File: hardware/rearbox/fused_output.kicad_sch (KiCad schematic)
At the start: 15 parts, among them U7 VND7020AJTR

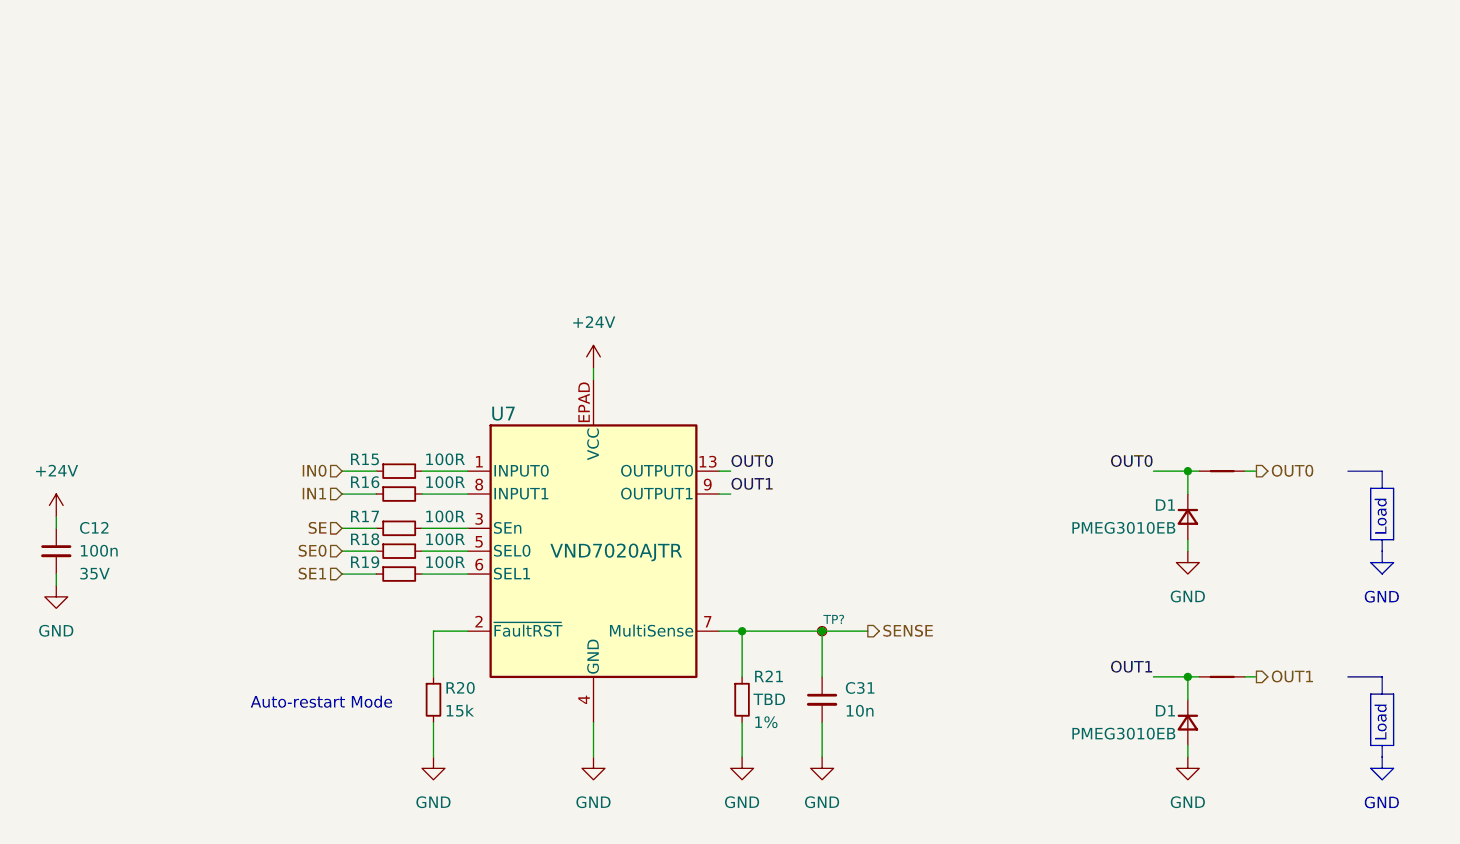
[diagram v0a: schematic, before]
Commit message: Place components on the PCB
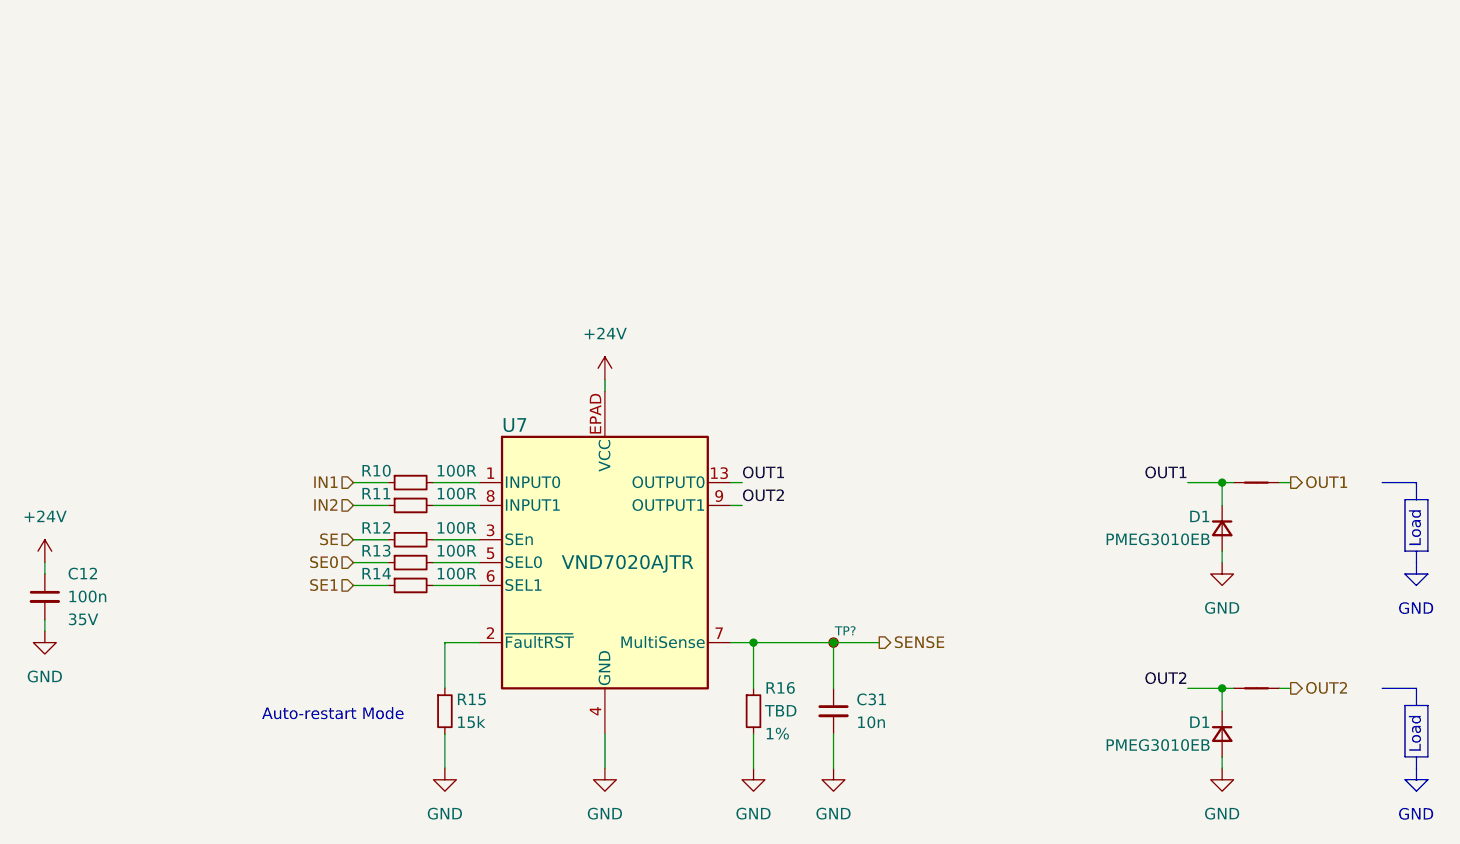
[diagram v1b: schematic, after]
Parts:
- renumbered R15 to R10, R16 to R11, R17 to R12, R18 to R13, R19 to R14, R20 to R15, R21 to R16
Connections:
- net IN0 is gone; now on net IN1: R10.1
- net OUT0 is gone; now on net OUT1: D1.1 (K), NT5.1, NT5.2, U7.13 (OUTPUT0), U7.14 (OUTPUT0), U7.15 (OUTPUT0), U7.16 (OUTPUT0)
- net IN1: no longer R11.1
- net OUT1: no longer D1.1 (K), NT5.1, NT5.2, U7.10 (OUTPUT1), U7.11 (OUTPUT1), U7.12 (OUTPUT1), U7.9 (OUTPUT1)
- new net IN2: R11.1
- new net OUT2: D1.1 (K), NT5.1, NT5.2, U7.10 (OUTPUT1), U7.11 (OUTPUT1), U7.12 (OUTPUT1), U7.9 (OUTPUT1)
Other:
- moved on the sheet: C12, C31, D1, R10, R11, R12, R13, R14, R15, R16, TP?, U7

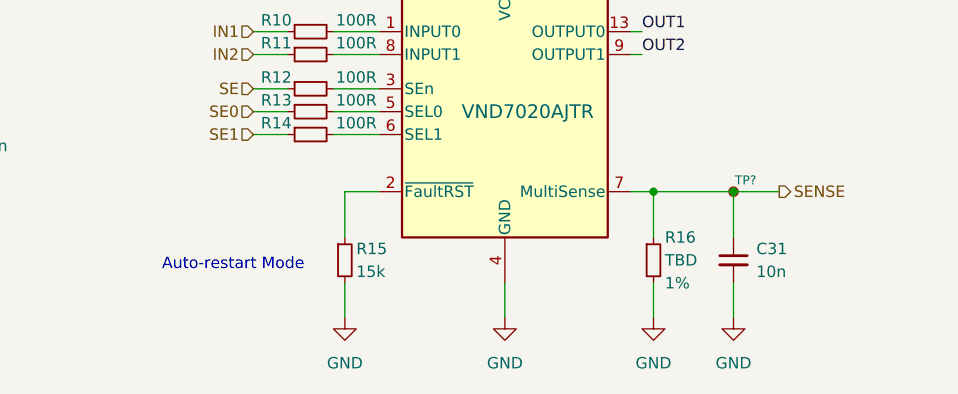
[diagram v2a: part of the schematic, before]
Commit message: Route PCB tracks
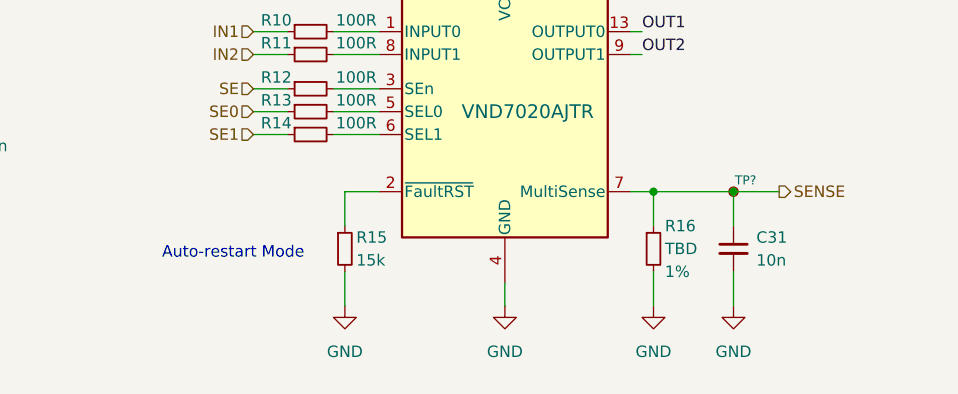
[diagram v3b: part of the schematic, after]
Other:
- moved on the sheet: C31, R15, R16
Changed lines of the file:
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@@
     (stroke (width 0) (type default))
   )
-  (wire (pts (xy 119.38 113.03) (xy 119.38 116.84))
+  (wire (pts (xy 119.38 111.76) (xy 119.38 115.57))
     (stroke (width 0) (type default))
   )
@@
     (stroke (width 0) (type default))
   )
-  (wire (pts (xy 162.56 102.87) (xy 162.56 107.95))
+  (wire (pts (xy 162.56 102.87) (xy 162.56 106.68))
     (stroke (width 0) (type default))
   )
@@
     (stroke (width 0) (type default))
   )
-  (wire (pts (xy 162.56 113.03) (xy 162.56 116.84))
-    (stroke (width 0) (type default))
-  )
-  (wire (pts (xy 153.67 102.87) (xy 153.67 107.95))
+  (wire (pts (xy 162.56 111.76) (xy 162.56 115.57))
+    (stroke (width 0) (type default))
+  )
+  (wire (pts (xy 153.67 102.87) (xy 153.67 106.68))
     (stroke (width 0) (type default))
   )
@@
     (stroke (width 0) (type default))
   )
-  (wire (pts (xy 137.16 113.03) (xy 137.16 116.84))
+  (wire (pts (xy 137.16 113.03) (xy 137.16 115.57))
     (stroke (width 0) (type default))
   )
@@
     (stroke (width 0) (type default))
   )
+  (wire (pts (xy 153.67 111.76) (xy 153.67 115.57))
+    (stroke (width 0) (type default))
+  )
   (polyline (pts (xy 223.52 85.09) (xy 227.33 85.09))
     (stroke (width 0) (type default))
@@
     (stroke (width 0) (type default))
   )
-  (wire (pts (xy 119.38 102.87) (xy 119.38 107.95))
+  (wire (pts (xy 119.38 102.87) (xy 119.38 106.68))
     (stroke (width 0) (type default))
   )
@@
   )
   (wire (pts (xy 153.67 102.87) (xy 162.56 102.87))
-    (stroke (width 0) (type default))
-  )
-  (wire (pts (xy 153.67 113.03) (xy 153.67 116.84))
     (stroke (width 0) (type default))
   )
@@
     (effects (font (size 1.27 1.27)) (justify left bottom))
   )
-  (text "Auto-restart Mode" (at 99.06 111.76 0)
+  (text "Auto-restart Mode" (at 99.06 110.49 0)
     (effects (font (size 1.27 1.27)) (justify left bottom))
   )
@@
     )
   )
-  (symbol (lib_id "power:GND") (at 162.56 116.84 0) (unit 1)
-    (in_bom yes) (on_board yes) (dnp no)
-    (property "Reference" "#PWR?" (at 162.56 123.19 0)
-      (effects (font (size 1.27 1.27)) hide)
-    )
-    (property "Value" "GND" (at 162.56 121.92 0)
-      (effects (font (size 1.27 1.27)))
-    )
-    (property "Footprint" "" (at 162.56 116.84 0)
-      (effects (font (size 1.27 1.27)) hide)
-    )
-    (property "Datasheet" "" (at 162.56 116.84 0)
+  (symbol (lib_id "power:GND") (at 162.56 115.57 0) (unit 1)
+    (in_bom yes) (on_board yes) (dnp no)
+    (property "Reference" "#PWR?" (at 162.56 121.92 0)
+      (effects (font (size 1.27 1.27)) hide)
+    )
+    (property "Value" "GND" (at 162.56 120.65 0)
+      (effects (font (size 1.27 1.27)))
+    )
+    (property "Footprint" "" (at 162.56 115.57 0)
+      (effects (font (size 1.27 1.27)) hide)
+    )
+    (property "Datasheet" "" (at 162.56 115.57 0)
       (effects (font (size 1.27 1.27)) hide)
     )
@@
     )
   )
-  (symbol (lib_id "Device:R_Small") (at 153.67 110.49 0) (unit 1)
-    (in_bom yes) (on_board yes) (dnp no)
-    (property "Reference" "R16" (at 154.94 107.95 0)
+  (symbol (lib_id "Device:R_Small") (at 153.67 109.22 0) (unit 1)
+    (in_bom yes) (on_board yes) (dnp no)
+    (property "Reference" "R16" (at 154.94 106.68 0)
       (effects (font (size 1.27 1.27)) (justify left))
     )
-    (property "Value" "TBD" (at 154.94 110.49 0)
+    (property "Value" "TBD" (at 154.94 109.22 0)
       (effects (font (size 1.27 1.27)) (justify left))
     )
-    (property "Footprint" "Resistor_SMD:R_0603_1608Metric" (at 153.67 110.49 0)
-      (effects (font (size 1.27 1.27)) hide)
-    )
-    (property "Datasheet" "~" (at 153.67 110.49 0)
-      (effects (font (size 1.27 1.27)) hide)
-    )
-    (property "Tolerance" "1%" (at 154.94 113.03 0)
+    (property "Footprint" "Resistor_SMD:R_0603_1608Metric" (at 153.67 109.22 0)
+      (effects (font (size 1.27 1.27)) hide)
+    )
+    (property "Datasheet" "~" (at 153.67 109.22 0)
+      (effects (font (size 1.27 1.27)) hide)
+    )
+    (property "Tolerance" "1%" (at 154.94 111.76 0)
       (effects (font (size 1.27 1.27)) (justify left))
     )
@@
     )
   )
-  (symbol (lib_id "power:GND") (at 153.67 116.84 0) (unit 1)
-    (in_bom yes) (on_board yes) (dnp no)
-    (property "Reference" "#PWR?" (at 153.67 123.19 0)
-      (effects (font (size 1.27 1.27)) hide)
-    )
-    (property "Value" "GND" (at 153.67 121.92 0)
-      (effects (font (size 1.27 1.27)))
-    )
-    (property "Footprint" "" (at 153.67 116.84 0)
-      (effects (font (size 1.27 1.27)) hide)
-    )
-    (property "Datasheet" "" (at 153.67 116.84 0)
+  (symbol (lib_id "power:GND") (at 153.67 115.57 0) (unit 1)
+    (in_bom yes) (on_board yes) (dnp no)
+    (property "Reference" "#PWR?" (at 153.67 121.92 0)
+      (effects (font (size 1.27 1.27)) hide)
+    )
+    (property "Value" "GND" (at 153.67 120.65 0)
+      (effects (font (size 1.27 1.27)))
+    )
+    (property "Footprint" "" (at 153.67 115.57 0)
+      (effects (font (size 1.27 1.27)) hide)
+    )
+    (property "Datasheet" "" (at 153.67 115.57 0)
       (effects (font (size 1.27 1.27)) hide)
     )
@@
     )
   )
-  (symbol (lib_id "Device:R_Small") (at 119.38 110.49 0) (unit 1)
-    (in_bom yes) (on_board yes) (dnp no)
-    (property "Reference" "R15" (at 120.65 109.22 0)
+  (symbol (lib_id "Device:R_Small") (at 119.38 109.22 0) (unit 1)
+    (in_bom yes) (on_board yes) (dnp no)
+    (property "Reference" "R15" (at 120.65 107.95 0)
       (effects (font (size 1.27 1.27)) (justify left))
     )
-    (property "Value" "15k" (at 120.65 111.76 0)
+    (property "Value" "15k" (at 120.65 110.49 0)
       (effects (font (size 1.27 1.27)) (justify left))
     )
-    (property "Footprint" "Resistor_SMD:R_0603_1608Metric" (at 119.38 110.49 0)
-      (effects (font (size 1.27 1.27)) hide)
-    )
-    (property "Datasheet" "~" (at 119.38 110.49 0)
+    (property "Footprint" "Resistor_SMD:R_0603_1608Metric" (at 119.38 109.22 0)
+      (effects (font (size 1.27 1.27)) hide)
+    )
+    (property "Datasheet" "~" (at 119.38 109.22 0)
       (effects (font (size 1.27 1.27)) hide)
     )
@@
     )
   )
-  (symbol (lib_id "power:GND") (at 137.16 116.84 0) (unit 1)
-    (in_bom yes) (on_board yes) (dnp no)
-    (property "Reference" "#PWR?" (at 137.16 123.19 0)
-      (effects (font (size 1.27 1.27)) hide)
-    )
-    (property "Value" "GND" (at 137.16 121.92 0)
-      (effects (font (size 1.27 1.27)))
-    )
-    (property "Footprint" "" (at 137.16 116.84 0)
-      (effects (font (size 1.27 1.27)) hide)
-    )
-    (property "Datasheet" "" (at 137.16 116.84 0)
+  (symbol (lib_id "power:GND") (at 137.16 115.57 0) (unit 1)
+    (in_bom yes) (on_board yes) (dnp no)
+    (property "Reference" "#PWR?" (at 137.16 121.92 0)
+      (effects (font (size 1.27 1.27)) hide)
+    )
+    (property "Value" "GND" (at 137.16 120.65 0)
+      (effects (font (size 1.27 1.27)))
+    )
+    (property "Footprint" "" (at 137.16 115.57 0)
+      (effects (font (size 1.27 1.27)) hide)
+    )
+    (property "Datasheet" "" (at 137.16 115.57 0)
       (effects (font (size 1.27 1.27)) hide)
     )
@@
     )
   )
-  (symbol (lib_id "power:GND") (at 119.38 116.84 0) (unit 1)
-    (in_bom yes) (on_board yes) (dnp no)
-    (property "Reference" "#PWR?" (at 119.38 123.19 0)
-      (effects (font (size 1.27 1.27)) hide)
-    )
-    (property "Value" "GND" (at 119.38 121.92 0)
-      (effects (font (size 1.27 1.27)))
-    )
-    (property "Footprint" "" (at 119.38 116.84 0)
-      (effects (font (size 1.27 1.27)) hide)
-    )
-    (property "Datasheet" "" (at 119.38 116.84 0)
+  (symbol (lib_id "power:GND") (at 119.38 115.57 0) (unit 1)
+    (in_bom yes) (on_board yes) (dnp no)
+    (property "Reference" "#PWR?" (at 119.38 121.92 0)
+      (effects (font (size 1.27 1.27)) hide)
+    )
+    (property "Value" "GND" (at 119.38 120.65 0)
+      (effects (font (size 1.27 1.27)))
+    )
+    (property "Footprint" "" (at 119.38 115.57 0)
+      (effects (font (size 1.27 1.27)) hide)
+    )
+    (property "Datasheet" "" (at 119.38 115.57 0)
       (effects (font (size 1.27 1.27)) hide)
     )
@@
     )
   )
-  (symbol (lib_id "Device:C_Small") (at 162.56 110.49 0) (unit 1)
+  (symbol (lib_id "Device:C_Small") (at 162.56 109.22 0) (unit 1)
     (in_bom yes) (on_board yes) (dnp no) (fields_autoplaced)
-    (property "Reference" "C31" (at 165.1 109.2263 0)
+    (property "Reference" "C31" (at 165.1 107.9563 0)
       (effects (font (size 1.27 1.27)) (justify left))
     )
-    (property "Value" "10n" (at 165.1 111.7663 0)
+    (property "Value" "10n" (at 165.1 110.4963 0)
       (effects (font (size 1.27 1.27)) (justify left))
     )
-    (property "Footprint" "Capacitor_SMD:C_0603_1608Metric" (at 162.56 110.49 0)
-      (effects (font (size 1.27 1.27)) hide)
-    )
-    (property "Datasheet" "~" (at 162.56 110.49 0)
-      (effects (font (size 1.27 1.27)) hide)
-    )
+    (property "Footprint" "Capacitor_SMD:C_0603_1608Metric" (at 162.56 109.22 0)
+      (effects (font (size 1.27 1.27)) hide)
+    )
+    (property "Datasheet" "~" (at 162.56 109.22 0)
+      (effects (font (size 1.27 1.27)) hide)
+    )

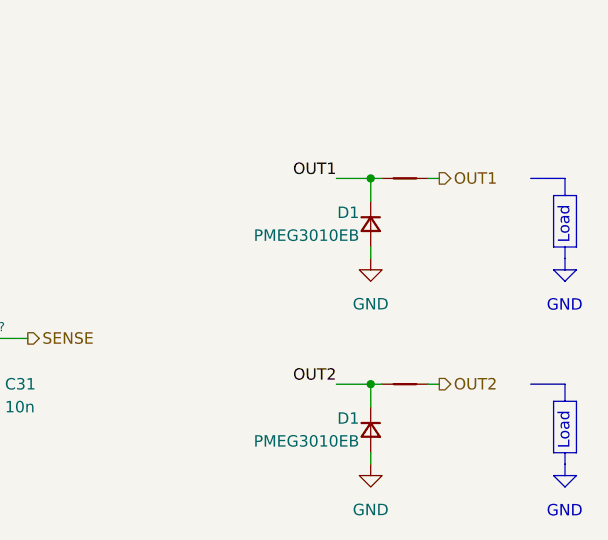
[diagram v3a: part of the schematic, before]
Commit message: Fix DRCs
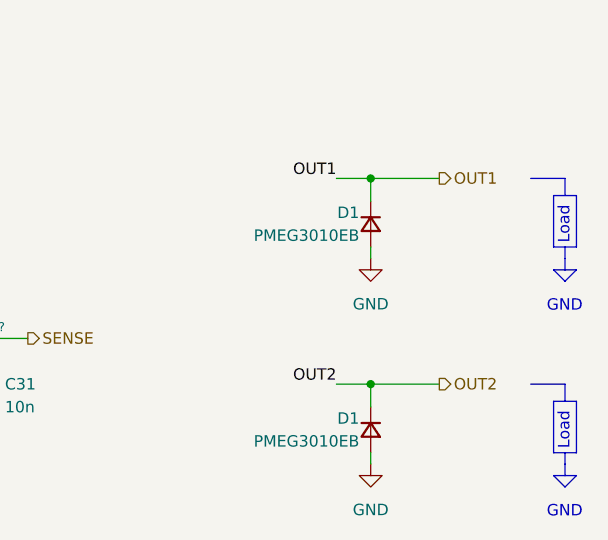
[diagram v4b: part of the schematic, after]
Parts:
- removed NT5 (x2): NetTie_2, NetTie:NetTie-2_SMD_Pad0.5mm, symbol Device:NetTie_2
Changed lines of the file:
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@@
   (title_block
     (title "Fans")
-    (date "2023-11-02")
+    (date "2023-11-17")
     (rev "${REVISION}")
     (company "Author: I. Kajdan")
@@
     (stroke (width 0) (type default))
   )
-  (wire (pts (xy 205.74 85.09) (xy 207.01 85.09))
-    (stroke (width 0) (type default))
-  )
   (polyline (pts (xy 226.06 95.25) (xy 227.33 95.25))
     (stroke (width 0) (type default))
@@
     (stroke (width 0) (type default))
   )
-  (wire (pts (xy 212.09 85.09) (xy 213.36 85.09))
+  (wire (pts (xy 205.74 85.09) (xy 213.36 85.09))
     (stroke (width 0) (type default))
   )
@@
     (stroke (width 0) (type default))
   )
-  (wire (pts (xy 212.09 107.95) (xy 213.36 107.95))
-    (stroke (width 0) (type default))
-  )
   (wire (pts (xy 205.74 85.09) (xy 205.74 87.63))
     (stroke (width 0) (type default))
@@
     (stroke (width 0) (type default))
   )
-  (wire (pts (xy 205.74 107.95) (xy 207.01 107.95))
+  (wire (pts (xy 205.74 107.95) (xy 213.36 107.95))
     (stroke (width 0) (type default))
   )
@@
     )
   )
-  (symbol (lib_id "Device:NetTie_2") (at 209.55 85.09 0) (unit 1)
-    (in_bom no) (on_board yes) (dnp no) (fields_autoplaced)
-    (property "Reference" "NT5" (at 209.55 80.01 0)
-      (effects (font (size 1.27 1.27)) hide)
-    )
-    (property "Value" "NetTie_2" (at 209.55 82.55 0)
-      (effects (font (size 1.27 1.27)) hide)
-    )
-    (property "Footprint" "NetTie:NetTie-2_SMD_Pad0.5mm" (at 209.55 85.09 0)
-      (effects (font (size 1.27 1.27)) hide)
-    )
-    (property "Datasheet" "~" (at 209.55 85.09 0)
-      (effects (font (size 1.27 1.27)) hide)
-    )
-    (pin "1")
-    (pin "2")
-    (instances
-      (project "rearbox"
-        (path "/b652b05a-4e3d-4ad1-b032-18886abe7d45/620acd23-76d3-49a1-9dab-637cd753e552"
-          (reference "NT5") (unit 1)
-        )
-        (path "/b652b05a-4e3d-4ad1-b032-18886abe7d45/12f12a63-cabc-40cf-a64b-d1bd8b3dd459"
-          (reference "NT1") (unit 1)
-        )
-        (path "/b652b05a-4e3d-4ad1-b032-18886abe7d45/2f82735d-d185-44cc-bb86-fc399780134d"
-          (reference "NT3") (unit 1)
-        )
-      )
-    )
-  )
   (symbol (lib_id "power:GND") (at 153.67 115.57 0) (unit 1)
     (in_bom yes) (on_board yes) (dnp no)
@@
         )
       )
-    )
-  )
-  (symbol (lib_id "Device:NetTie_2") (at 209.55 107.95 0) (unit 1)
-    (in_bom no) (on_board yes) (dnp no) (fields_autoplaced)
-    (property "Reference" "NT5" (at 209.55 102.87 0)
-      (effects (font (size 1.27 1.27)) hide)
-    )
-    (property "Value" "NetTie_2" (at 209.55 105.41 0)
-      (effects (font (size 1.27 1.27)) hide)
-    )
-    (property "Footprint" "NetTie:NetTie-2_SMD_Pad0.5mm" (at 209.55 107.95 0)
-      (effects (font (size 1.27 1.27)) hide)
-    )
-    (property "Datasheet" "~" (at 209.55 107.95 0)
-      (effects (font (size 1.27 1.27)) hide)
-    )
-    (pin "1")
-    (pin "2")
-    (instances
-      (project "rearbox"
-        (path "/b652b05a-4e3d-4ad1-b032-18886abe7d45/620acd23-76d3-49a1-9dab-637cd753e552"
-          (reference "NT5") (unit 1)
-        )
-        (path "/b652b05a-4e3d-4ad1-b032-18886abe7d45/12f12a63-cabc-40cf-a64b-d1bd8b3dd459"
-          (reference "NT2") (unit 1)
-        )
-        (path "/b652b05a-4e3d-4ad1-b032-18886abe7d45/2f82735d-d185-44cc-bb86-fc399780134d"
-          (reference "NT4") (unit 1)
-        )
-      )
